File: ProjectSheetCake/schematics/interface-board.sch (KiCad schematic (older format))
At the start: 44 parts, among them P1 CONN_8, P2 CONN_6, P3 CONN_8, P4 CONN_6, P7 X_Y_SERVO, P8 Z_A_SERVO

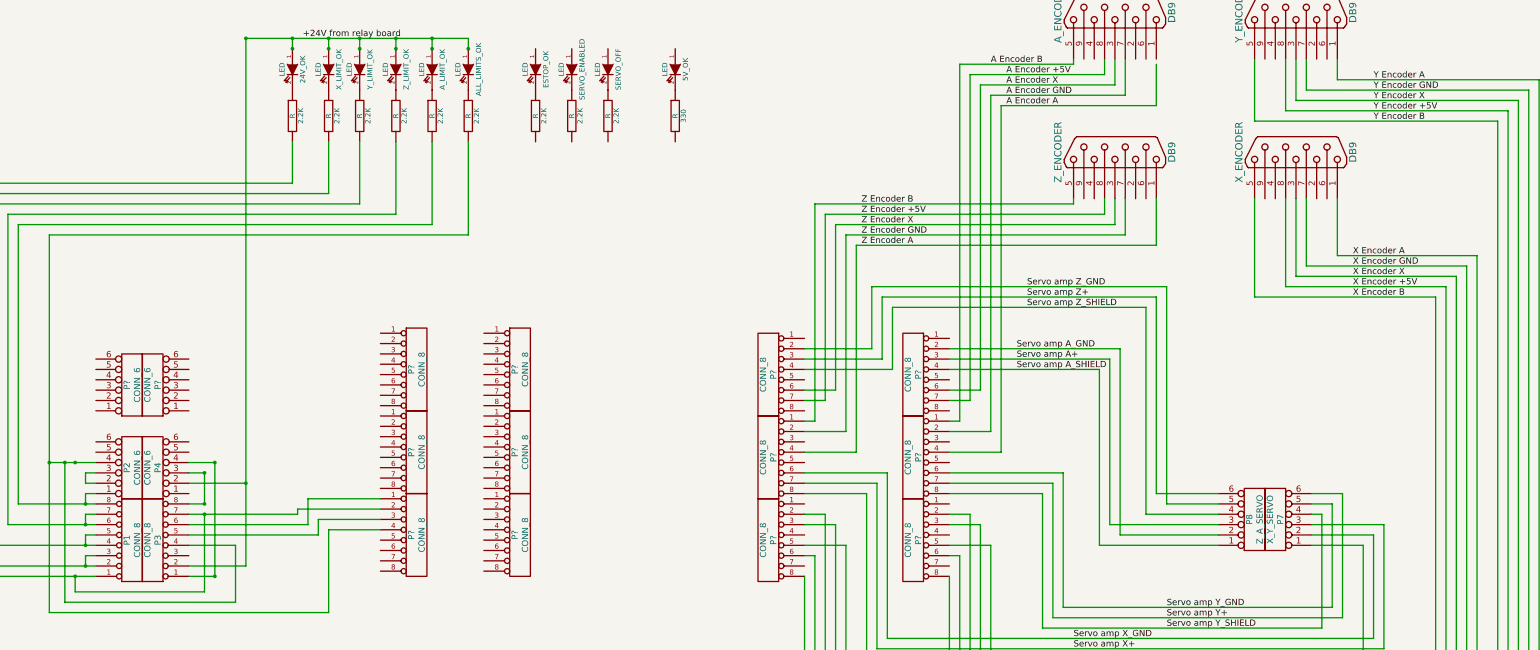
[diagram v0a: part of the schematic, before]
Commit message: minor updates to encoder labels to match Mesa docs
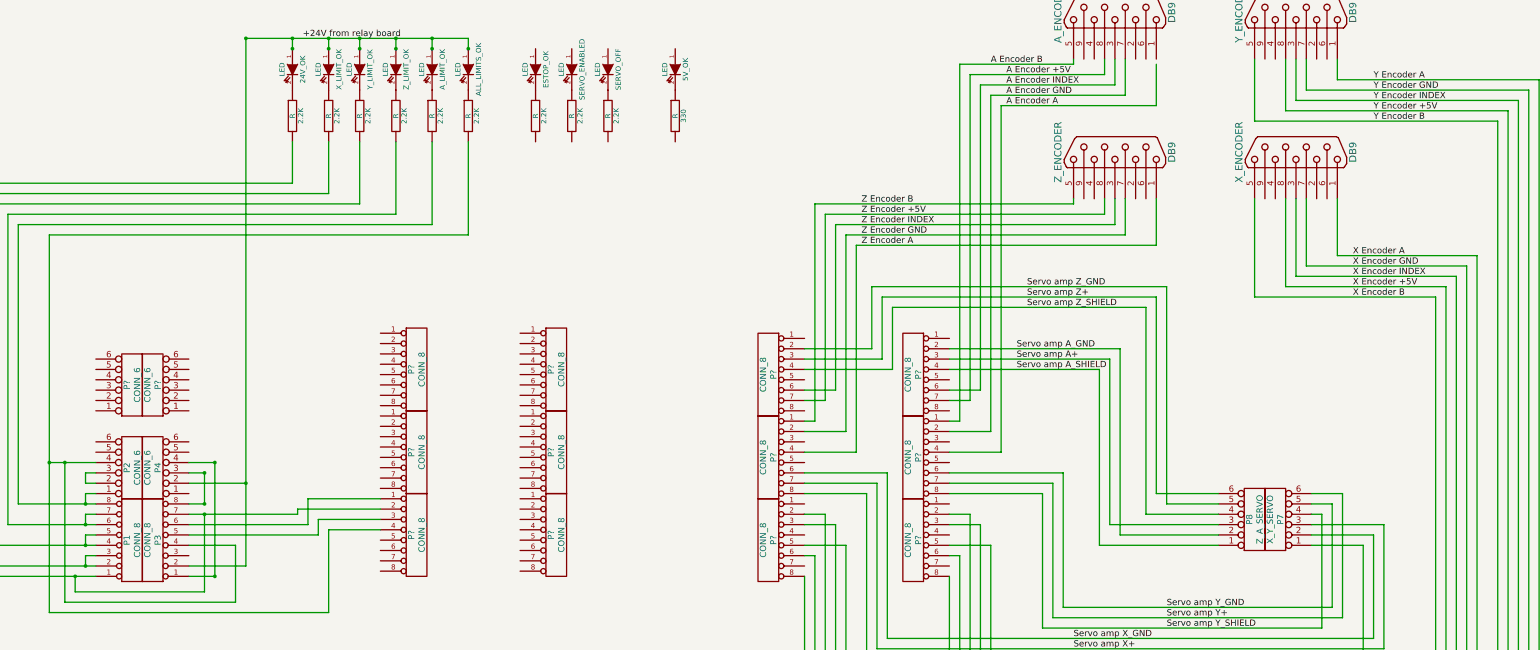
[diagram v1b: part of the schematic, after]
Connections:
- net labels added: A Encoder INDEX, X Encoder INDEX, Y Encoder INDEX, Z Encoder INDEX
- net labels removed: A Encoder X, X Encoder X, Y Encoder X, Z Encoder X
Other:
- moved on the sheet: P?
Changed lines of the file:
@@
-EESchema Schematic File Version 2  date 8/12/2011 11:07:03 PM
+EESchema Schematic File Version 2  date 8/12/2011 11:33:44 PM
 LIBS:power
 LIBS:device
@@
 Wire Wire Line
 	1800 5400 2250 5400
-Connection ~ 2050 5400
 Wire Wire Line
 	4400 5950 4400 6100
@@
 Z Encoder GND
 Text Label 9650 3100 0    60   ~ 0
-Z Encoder X
+Z Encoder INDEX
 Text Label 9650 3000 0    60   ~ 0
 Z Encoder +5V
@@
 A Encoder +5V
 Text Label 11050 1750 0    60   ~ 0
-A Encoder X
+A Encoder INDEX
 Text Label 11050 1850 0    60   ~ 0
 A Encoder GND
@@
 Y Encoder +5V
 Text Label 14600 1900 0    60   ~ 0
-Y Encoder X
+Y Encoder INDEX
 Text Label 14600 1800 0    60   ~ 0
 Y Encoder GND
@@
 X Encoder +5V
 Text Label 14400 3600 0    60   ~ 0
-X Encoder X
+X Encoder INDEX
 Text Label 14400 3500 0    60   ~ 0
 X Encoder GND
@@
 L CONN_8 P?
 U 1 1 4E3F5325
-P 6350 6100
-F 0 "P?" V 6300 6100 60  0000 C CNN
-F 1 "CONN_8" V 6400 6100 60  0000 C CNN
-	1    6350 6100
+P 6700 6100
+F 0 "P?" V 6650 6100 60  0000 C CNN
+F 1 "CONN_8" V 6750 6100 60  0000 C CNN
+	1    6700 6100
 	1    0    0    -1
 $EndComp
@@
 L CONN_8 P?
 U 1 1 4E3F5321
-P 6350 5300
-F 0 "P?" V 6300 5300 60  0000 C CNN
-F 1 "CONN_8" V 6400 5300 60  0000 C CNN
-	1    6350 5300
+P 6700 5300
+F 0 "P?" V 6650 5300 60  0000 C CNN
+F 1 "CONN_8" V 6750 5300 60  0000 C CNN
+	1    6700 5300
 	1    0    0    -1
 $EndComp
@@
 L CONN_8 P?
 U 1 1 4E3F531C
-P 6350 4500
-F 0 "P?" V 6300 4500 60  0000 C CNN
-F 1 "CONN_8" V 6400 4500 60  0000 C CNN
-	1    6350 4500
-	1    0    0    -1
-$EndComp
+P 6700 4500
+F 0 "P?" V 6650 4500 60  0000 C CNN
+F 1 "CONN_8" V 6750 4500 60  0000 C CNN
+	1    6700 4500
+	1    0    0    -1
+$EndComp

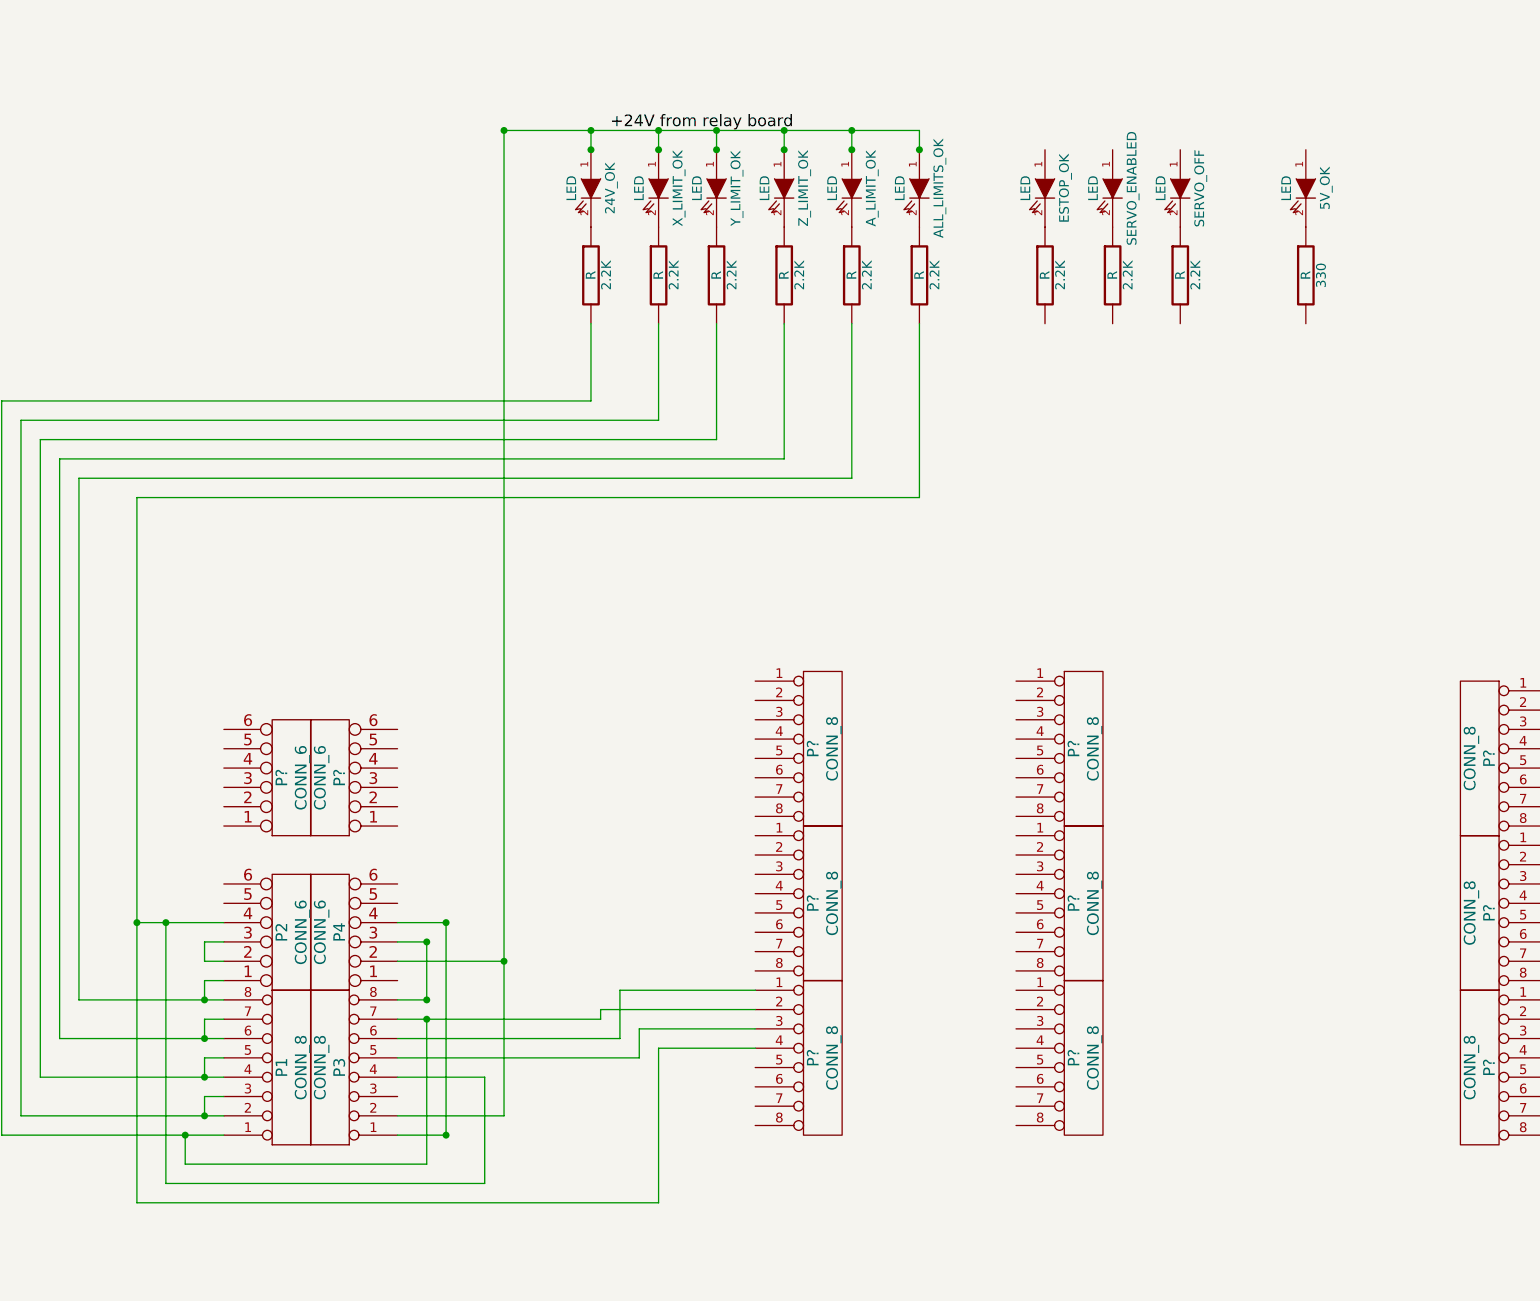
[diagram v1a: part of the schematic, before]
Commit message: added LED routing
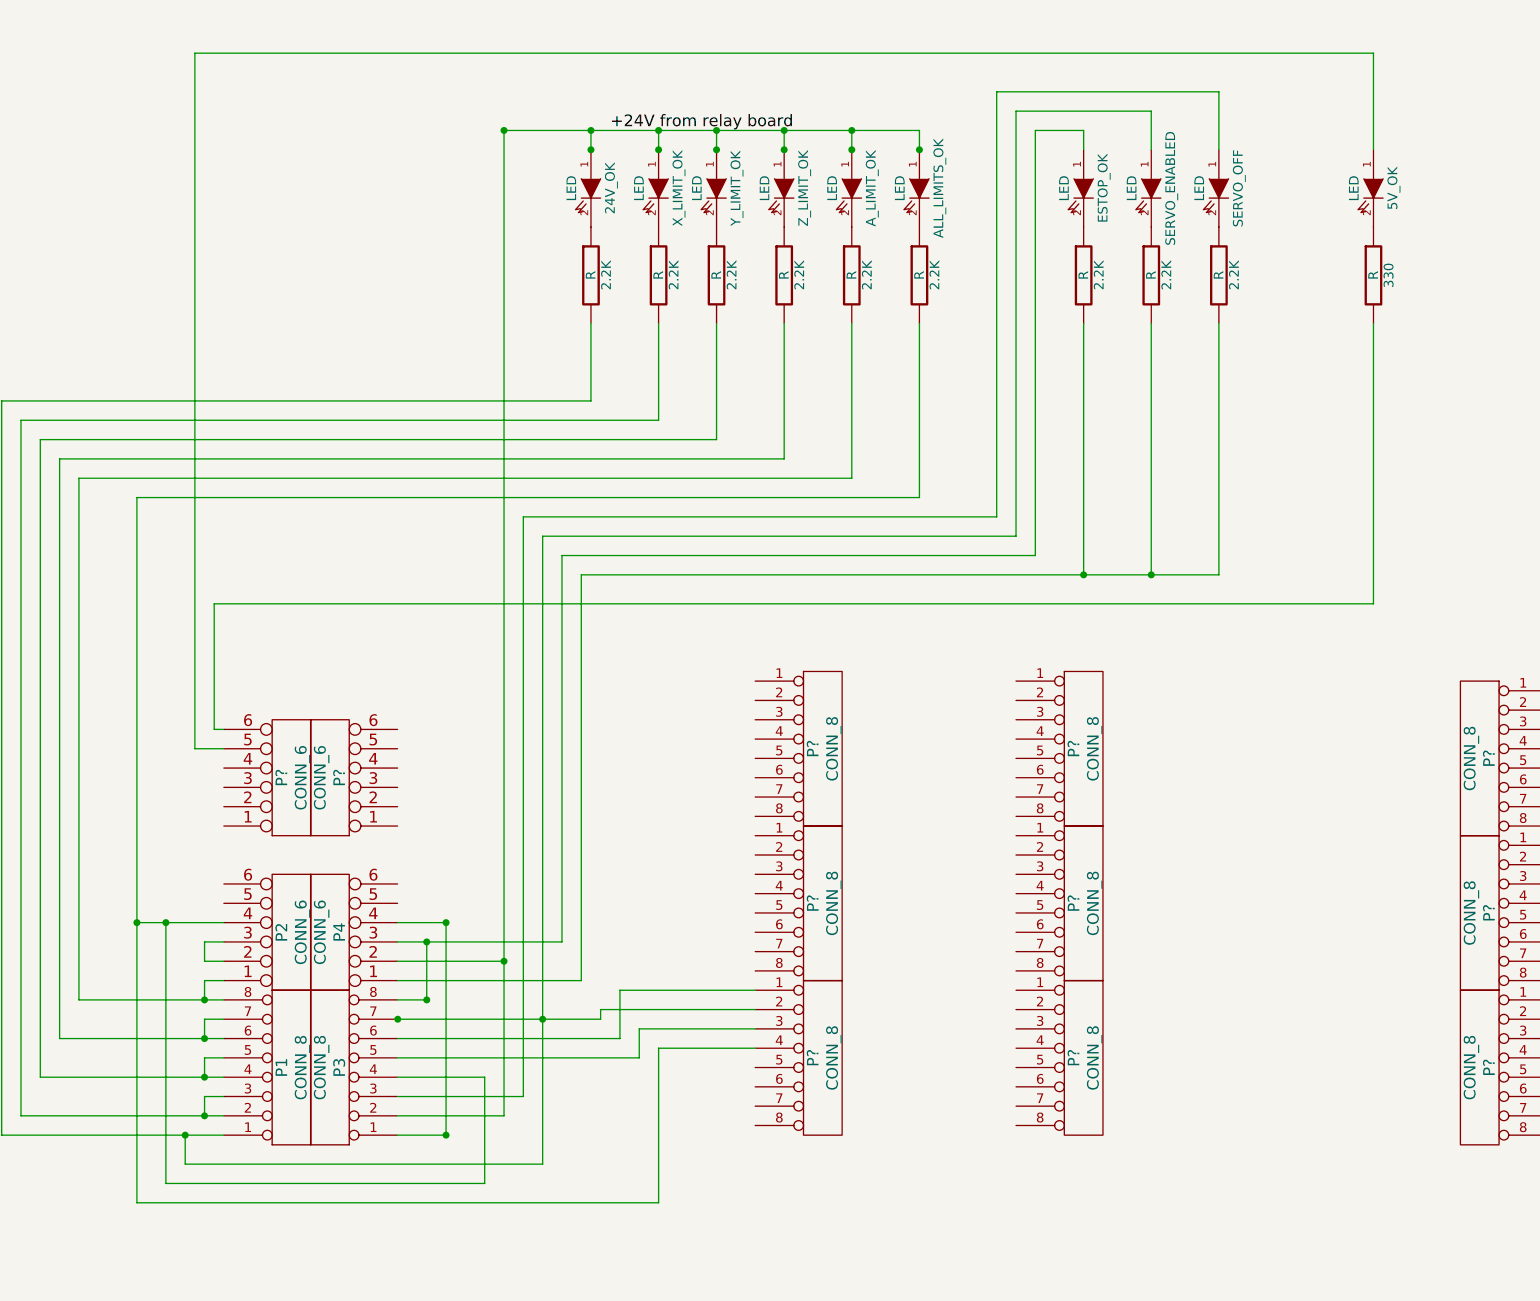
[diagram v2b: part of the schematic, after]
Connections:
- wire segments 223 -> 252
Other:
- moved on the sheet: 2.2K, 330, 5V_OK, ESTOP_OK, SERVO_ENABLED, SERVO_OFF
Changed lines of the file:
@@
-EESchema Schematic File Version 2  date 8/12/2011 11:33:44 PM
+EESchema Schematic File Version 2  date 8/12/2011 11:43:42 PM
 LIBS:power
 LIBS:device
@@
 Comment4 ""
 $EndDescr
-Text Label 11250 3900 0    60   ~ 0
-Servo amp Z_SHIELD
-Text Label 11250 3800 0    60   ~ 0
-Servo amp Z+
-Text Label 11250 3700 0    60   ~ 0
-Servo amp Z_GND
+Wire Wire Line
+	2250 4500 2100 4500
+Wire Wire Line
+	2100 4500 2100 900
+Wire Wire Line
+	2100 900  8200 900
+Wire Wire Line
+	8200 900  8200 1400
+Connection ~ 3900 5900
+Wire Wire Line
+	3900 3400 6350 3400
+Wire Wire Line
+	7400 1400 7400 1100
+Wire Wire Line
+	7400 1100 6250 1100
+Wire Wire Line
+	6250 1100 6250 3300
+Wire Wire Line
+	6250 3300 3800 3300
+Wire Wire Line
+	3800 3300 3800 6300
+Wire Wire Line
+	3800 6300 3150 6300
+Wire Wire Line
+	7050 3600 7050 2300
+Wire Wire Line
+	4100 5700 4100 3600
+Wire Wire Line
+	6700 1400 6700 1300
+Wire Wire Line
+	6700 1300 6450 1300
+Wire Wire Line
+	6450 1300 6450 3500
+Wire Wire Line
+	4000 5500 4000 3500
+Wire Wire Line
+	4000 5500 3300 5500
 Wire Wire Line
 	9950 3900 9950 4500
@@
 Connection ~ 3300 5500
 Connection ~ 3300 5800
-Connection ~ 3300 5900
 Wire Wire Line
 	5000 5850 4200 5850
 Wire Wire Line
 	4200 5850 4200 5900
-Wire Wire Line
-	4200 5900 3300 5900
 Connection ~ 1950 5400
 Wire Wire Line
@@
 	3600 6200 3150 6200
 Wire Wire Line
-	3300 6650 2050 6650
-Wire Wire Line
 	3150 6100 4400 6100
 Wire Wire Line
@@
 	3299 5500 3149 5500
 Wire Wire Line
-	3300 5800 3300 5500
+	3300 5500 3300 5800
 Wire Wire Line
 	3149 5800 3299 5800
@@
 	2150 5700 2250 5700
 Wire Wire Line
-	3299 5900 3149 5900
-Wire Wire Line
-	3300 6650 3300 5900
-Wire Wire Line
 	3399 5400 3149 5400
 Wire Wire Line
@@
 	4500 6850 1800 6850
 Wire Wire Line
-	1800 5400 2250 5400
+	2250 5400 1800 5400
 Wire Wire Line
 	4400 5950 4400 6100
 Wire Wire Line
-	2050 6650 2050 6500
+	2050 6500 2050 6650
 Wire Wire Line
 	3150 6000 4300 6000
@@
 Connection ~ 4150 1300
 Wire Wire Line
-	4800 1400 4800 1300
+	4800 1300 4800 1400
 Connection ~ 4800 1300
 Wire Wire Line
-	5500 1400 5500 1300
+	5500 1300 5500 1400
 Connection ~ 5500 1300
 Wire Wire Line
@@
 Wire Wire Line
 	9850 3800 9850 4400
+Wire Wire Line
+	6700 3600 6700 2300
+Wire Wire Line
+	4100 5700 3150 5700
+Wire Wire Line
+	7400 2300 7400 3600
+Wire Wire Line
+	4000 3500 6450 3500
+Wire Wire Line
+	7400 3600 4100 3600
+Connection ~ 7050 3600
+Connection ~ 6700 3600
+Wire Wire Line
+	3900 3400 3900 6650
+Wire Wire Line
+	6350 3400 6350 1200
+Wire Wire Line
+	6350 1200 7050 1200
+Wire Wire Line
+	7050 1200 7050 1400
+Connection ~ 3150 5900
+Wire Wire Line
+	4200 5900 3150 5900
+Wire Wire Line
+	3900 6650 2050 6650
+Wire Wire Line
+	2250 4400 2200 4400
+Wire Wire Line
+	2200 4400 2200 3750
+Wire Wire Line
+	2200 3750 8200 3750
+Wire Wire Line
+	8200 3750 8200 2300
+Text Label 11250 3900 0    60   ~ 0
+Servo amp Z_SHIELD
+Text Label 11250 3800 0    60   ~ 0
+Servo amp Z+
+Text Label 11250 3700 0    60   ~ 0
+Servo amp Z_GND
 Text Label 11150 4500 0    60   ~ 0
 Servo amp A_SHIELD
@@
 L R 2.2K
 U 1 1 4E45E9E2
-P 6500 2050
-F 0 "2.2K" V 6580 2050 50  0000 C CNN
-F 1 "R" V 6500 2050 50  0000 C CNN
-	1    6500 2050
+P 6700 2050
+F 0 "2.2K" V 6780 2050 50  0000 C CNN
+F 1 "R" V 6700 2050 50  0000 C CNN
+	1    6700 2050
 	1    0    0    -1
 $EndComp
@@
 L R 2.2K
 U 1 1 4E45E9E1
-P 6850 2050
-F 0 "2.2K" V 6930 2050 50  0000 C CNN
-F 1 "R" V 6850 2050 50  0000 C CNN
-	1    6850 2050
+P 7050 2050
+F 0 "2.2K" V 7130 2050 50  0000 C CNN
+F 1 "R" V 7050 2050 50  0000 C CNN
+	1    7050 2050
 	1    0    0    -1
 $EndComp
@@
 L R 2.2K
 U 1 1 4E45E9E0
-P 7200 2050
-F 0 "2.2K" V 7280 2050 50  0000 C CNN
-F 1 "R" V 7200 2050 50  0000 C CNN
-	1    7200 2050
+P 7400 2050
+F 0 "2.2K" V 7480 2050 50  0000 C CNN
+F 1 "R" V 7400 2050 50  0000 C CNN
+	1    7400 2050
 	1    0    0    -1
 $EndComp
@@
 L R 330
 U 1 1 4E45E288
-P 7850 2050
-F 0 "330" V 7930 2050 50  0000 C CNN
-F 1 "R" V 7850 2050 50  0000 C CNN
-	1    7850 2050
+P 8200 2050
+F 0 "330" V 8280 2050 50  0000 C CNN
+F 1 "R" V 8200 2050 50  0000 C CNN
+	1    8200 2050
 	1    0    0    -1
 $EndComp
@@
 L LED 5V_OK
 U 1 1 4E45E287
-P 7850 1600
-F 0 "5V_OK" H 7850 1700 50  0000 C CNN
-F 1 "LED" H 7850 1500 50  0000 C CNN
-	1    7850 1600
+P 8200 1600
+F 0 "5V_OK" H 8200 1700 50  0000 C CNN
+F 1 "LED" H 8200 1500 50  0000 C CNN
+	1    8200 1600
 	0    1    1    0
 $EndComp
@@
 L LED ESTOP_OK
 U 1 1 4E45E280
-P 6500 1600
-F 0 "ESTOP_OK" H 6500 1700 50  0000 C CNN
-F 1 "LED" H 6500 1500 50  0000 C CNN
-	1    6500 1600
+P 6700 1600
+F 0 "ESTOP_OK" H 6700 1700 50  0000 C CNN
+F 1 "LED" H 6700 1500 50  0000 C CNN
+	1    6700 1600
 	0    1    1    0
 $EndComp
@@
 L LED SERVO_ENABLED
 U 1 1 4E45E27E
-P 6850 1600
-F 0 "SERVO_ENABLED" H 6850 1700 50  0000 C CNN
-F 1 "LED" H 6850 1500 50  0000 C CNN
-	1    6850 1600
+P 7050 1600
+F 0 "SERVO_ENABLED" H 7050 1700 50  0000 C CNN
+F 1 "LED" H 7050 1500 50  0000 C CNN
+	1    7050 1600
 	0    1    1    0
 $EndComp
@@
 L LED SERVO_OFF
 U 1 1 4E45E27D
-P 7200 1600
-F 0 "SERVO_OFF" H 7200 1700 50  0000 C CNN
-F 1 "LED" H 7200 1500 50  0000 C CNN
-	1    7200 1600
+P 7400 1600
+F 0 "SERVO_OFF" H 7400 1700 50  0000 C CNN
+F 1 "LED" H 7400 1500 50  0000 C CNN
+	1    7400 1600
 	0    1    1    0
 $EndComp
